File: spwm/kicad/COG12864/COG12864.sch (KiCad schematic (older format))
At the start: 12 parts, among them U1 N32G430C8L7, Y1 8MHZ

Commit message: adc_采样
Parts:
- added C? (x6): C, symbol Device:C
- added C?: CP, symbol Device:CP
- added D? (x2): 1N47xxA, Diode_THT:D_DO-41_SOD81_P10.16mm_Horizontal, symbol COG12864-cache:1N47xxA
- added D? (x10): 1N4148, Diode_THT:D_DO-35_SOD27_P7.62mm_Horizontal, symbol Diode:1N4148
- added D? (x4): 1N47xxA, Diode_THT:D_DO-41_SOD81_P10.16mm_Horizontal, symbol Diode:1N47xxA
- added Q? (x4): Q_NMOS_GDS, symbol Device:Q_NMOS_GDS
- added Q? (x4): SS8550, Package_TO_SOT_THT:TO-92_Inline, symbol Transistor_BJT:S8550
- added Q? (x2): SS8050, Package_TO_SOT_THT:TO-92_Inline, symbol Transistor_BJT:S8050
- added R? (x32): R, symbol Device:R
- added R?: 100, symbol Device:R
- added R? (x2): 10K, symbol Device:R
- added T? (x2): Transformer_1P_2S, symbol Device:Transformer_1P_2S
- added U? (x6): LM358, symbol Amplifier_Operational:LM358
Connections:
- net labels added: ADC1, PA9_TIM1_CH2, SIN
- wire segments 63 -> 279
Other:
- note added: "~"
- moved on the sheet: C1, C2, C3, C4, C5, C6, D1, DS1, J?, R1, U1, Y1

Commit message: 采样
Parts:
- removed C? (x6): C, symbol Device:C
- removed R? (x10): R, symbol Device:R
- removed R? (x2): 10K, symbol Device:R
- removed U? (x4): LM358, symbol Amplifier_Operational:LM358
- added C10, C7: 106, symbol Device:C
- added C9: C, symbol Device:C
- added D2, D3, D4, D5: 1N4148, Diode_THT:D_DO-35_SOD27_P7.62mm_Horizontal, symbol Diode:1N4148
- added R10, R28: 1K, symbol Device:R
- added R2, R3: 100K, symbol Device:R
- R4, R5: renamed from R?; value R -> 100
- R6, R7: renamed from R?; value R -> 1K
- R8, R9: renamed from R?; value R -> 100K
- U2: renamed from U?; value LM358 -> LMV722
- gave numbers to parts that had none: 47
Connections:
- wire segments 279 -> 269
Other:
- moved on the sheet: R4, R5, U2C

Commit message: 修改方案
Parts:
- removed D10, D11, D16, D17, D18, D19, D21, D7, D8, D9: 1N4148, Diode_THT:D_DO-35_SOD27_P7.62mm_Horizontal, symbol Diode:1N4148
- removed D12, D13, D14, D15: 1N47xxA, Diode_THT:D_DO-41_SOD81_P10.16mm_Horizontal, symbol Diode:1N47xxA
- removed D20, D6: 1N47xxA, Diode_THT:D_DO-41_SOD81_P10.16mm_Horizontal, symbol COG12864-cache:1N47xxA
- removed Q1, Q10: SS8050, Package_TO_SOT_THT:TO-92_Inline, symbol Transistor_BJT:S8050
- removed Q2, Q3, Q8, Q9: SS8550, Package_TO_SOT_THT:TO-92_Inline, symbol Transistor_BJT:S8550
- removed R15, R16, R17, R18, R19, R20, R21, R22, R23, R24, R25, R26, R27: R, symbol Device:R
- removed T1, T2: Transformer_1P_2S, symbol Device:Transformer_1P_2S
- added C11, C14: 104, symbol Device:C
- added C12, C13: 106, symbol Device:C
- added D10, D11: FR107, symbol Device:D
- added D6, D7, D8, D9: 1N4007, Diode_THT:D_DO-41_SOD81_P10.16mm_Horizontal, symbol Diode:1N4007
- added U3, U4: EG2131, symbol Driver_FET:IR2103
- R11, R13, R14: value R -> 33
- R12: value 100 -> 33
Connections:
- net labels added: PB13_TIM1_CH1N, PB14_TIM1_CH2N
- wire segments 269 -> 209
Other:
- moved on the sheet: C1, C2, C3, C4, C5, C6, D1, DS1, R1, U1, Y1

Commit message: 锁相成功
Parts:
- removed U2: LMV722, symbol Amplifier_Operational:LM358
- added C16, C?: 470UF, symbol Device:CP
- added R15: 900, symbol Device:R
- added R17: 100, symbol Device:R
- added R? (x2): R, symbol Device:R
- added U5: LMV722, symbol COG12864-cache:LMV358
- added U6: LMV722, symbol Regulator_Linear:LM317_TO-220
- C8: value CP -> 470UF
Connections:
- net labels added: PB6_TIM4_CH1_guoling
- wire segments 209 -> 231
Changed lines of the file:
@@
 Text Label 1500 2300 0    354  ~ 71
 SIN
-$Comp
-L Amplifier_Operational:LM358 U2
-U 1 1 632E71DB
-P 5450 3300
-F 0 "U2" H 5450 3667 50  0000 C CNN
-F 1 "LMV722" H 5450 3576 50  0000 C CNN
-F 2 "" H 5450 3300 50  0001 C CNN
-F 3 "http://www.ti.com/lit/ds/symlink/lm2904-n.pdf" H 5450 3300 50  0001 C CNN
-	1    5450 3300
-	1    0    0    1
-$EndComp
-$Comp
-L Amplifier_Operational:LM358 U2
-U 3 1 632EB879
-P 5700 5250
-F 0 "U2" V 5800 5200 50  0000 L CNN
-F 1 "LMV722" V 5700 5150 50  0000 L CNN
-F 2 "" H 5700 5250 50  0001 C CNN
-F 3 "http://www.ti.com/lit/ds/symlink/lm2904-n.pdf" H 5700 5250 50  0001 C CNN
-	3    5700 5250
-	0    -1   -1   0
-$EndComp
 Wire Wire Line
 	4650 2750 4300 2750
@@
 Wire Wire Line
 	6050 5150 6050 4750
-Connection ~ 5750 3300
 Text Label 5950 3300 0    50   ~ 0
 ADC0
@@
 	12750 5650 13150 5650
 Wire Wire Line
-	12450 6650 11750 6650
-Wire Wire Line
 	11750 6650 11750 6400
 Wire Wire Line
@@
 Wire Wire Line
 	11300 5600 11300 5450
-Wire Wire Line
-	11300 5450 11250 5450
 Wire Wire Line
 	11700 5500 11700 5600
@@
 P 10650 3950
 F 0 "C8" V 10395 3950 50  0000 C CNN
-F 1 "CP" V 10486 3950 50  0000 C CNN
+F 1 "470UF" V 10486 3950 50  0000 C CNN
 F 2 "" H 10688 3800 50  0001 C CNN
 F 3 "~" H 10650 3950 50  0001 C CNN
@@
 Wire Wire Line
 	10800 3950 11150 3950
-Wire Wire Line
-	11150 3950 11150 3800
 Wire Wire Line
 	11150 3200 11050 3200
@@
 	10000 3850 10000 3200
 Wire Wire Line
-	11250 5450 11250 3800
-Wire Wire Line
-	11250 3800 11150 3800
-Connection ~ 11250 5450
-Wire Wire Line
-	11250 5450 10900 5450
-Connection ~ 11150 3800
-Wire Wire Line
-	11150 3800 11150 3200
-Wire Wire Line
-	13450 5450 15250 5450
-Wire Wire Line
-	13450 7350 14550 7350
-Text Label 10700 6100 2    50   ~ 0
+	13450 5450 14350 5450
+Wire Wire Line
+	13450 7350 14350 7350
+Text Label 11050 6150 2    50   ~ 0
 PA8_TIM1_CH1
-Text Label 10700 6200 2    50   ~ 0
-PB13_TIM1_CH1N
-Wire Wire Line
-	11150 6100 10700 6100
-Wire Wire Line
-	11150 6200 10700 6200
 $Comp
 L Driver_FET:IR2103 U4
@@
 Wire Wire Line
 	15250 6300 15250 6450
-Wire Wire Line
-	17450 3800 11250 3800
-Connection ~ 11250 3800
 $Comp
 L power:GND #PWR020
@@
 Text Label 18000 6200 0    50   ~ 0
 PB14_TIM1_CH2N
+Wire Wire Line
+	11150 6100 11050 6100
+Wire Wire Line
+	11050 6100 11050 6200
+Wire Wire Line
+	11050 6200 11150 6200
+Wire Wire Line
+	10900 5450 11300 5450
+Wire Wire Line
+	11150 3200 11150 3950
+$Comp
+L Regulator_Linear:LM317_TO-220 U6
+U 1 1 62FA851E
+P 11450 3950
+F 0 "U6" H 11450 4192 50  0000 C CNN
+F 1 "LMV722" H 11450 4101 50  0000 C CNN
+F 2 "" H 11450 4200 50  0001 C CIN
+F 3 "" H 11450 3950 50  0001 C CNN
+	1    11450 3950
+	1    0    0    -1
+$EndComp
+Connection ~ 11150 3950
+$Comp
+L Device:R R17
+U 1 1 62FAA4DC
+P 11850 4100
+F 0 "R17" H 11920 4146 50  0000 L CNN
+F 1 "100" H 11920 4055 50  0000 L CNN
+F 2 "" V 11780 4100 50  0001 C CNN
+F 3 "~" H 11850 4100 50  0001 C CNN
+	1    11850 4100
+	1    0    0    -1
+$EndComp
+$Comp
+L Device:R R15
+U 1 1 62FAB838
+P 11450 4450
+F 0 "R15" H 11520 4496 50  0000 L CNN
+F 1 "900" H 11520 4405 50  0000 L CNN
+F 2 "" V 11380 4450 50  0001 C CNN
+F 3 "~" H 11450 4450 50  0001 C CNN
+	1    11450 4450
+	1    0    0    -1
+$EndComp
+$Comp
+L power:GND #PWR023
+U 1 1 62FACA5A
+P 11600 4600
+F 0 "#PWR023" H 11600 4350 50  0001 C CNN
+F 1 "GND" H 11605 4427 50  0000 C CNN
+F 2 "" H 11600 4600 50  0001 C CNN
+F 3 "" H 11600 4600 50  0001 C CNN
+	1    11600 4600
+	1    0    0    -1
+$EndComp
+$Comp
+L Device:CP C16
+U 1 1 62FAEE23
+P 12250 4100
+F 0 "C16" H 12368 4146 50  0000 L CNN
+F 1 "470UF" H 12368 4055 50  0000 L CNN
+F 2 "" H 12288 3950 50  0001 C CNN
+F 3 "~" H 12250 4100 50  0001 C CNN
+	1    12250 4100
+	1    0    0    -1
+$EndComp
+Wire Wire Line
+	11850 4250 11450 4250
+Wire Wire Line
+	11450 4300 11450 4250
+Connection ~ 11450 4250
+Wire Wire Line
+	12250 4250 12250 4600
+Wire Wire Line
+	12250 4600 11600 4600
+Connection ~ 11600 4600
+Wire Wire Line
+	11600 4600 11450 4600
+Wire Wire Line
+	11750 3950 11850 3950
+Wire Wire Line
+	12750 3950 12750 5100
+Wire Wire Line
+	12750 5100 10900 5100
+Wire Wire Line
+	10900 5100 10900 5450
+Connection ~ 11850 3950
+Wire Wire Line
+	11850 3950 12250 3950
+Connection ~ 12250 3950
+Wire Wire Line
+	12250 3950 12750 3950
+Connection ~ 10900 5450
+Wire Wire Line
+	17450 3800 12750 3800
+Wire Wire Line
+	12750 3800 12750 3950
+Connection ~ 12750 3950
+$Comp
+L COG12864-cache:LMV358 U5
+U 1 1 63029AA7
+P 5450 3300
+F 0 "U5" H 5450 2933 50  0000 C CNN
+F 1 "LMV722" H 5450 3024 50  0000 C CNN
+F 2 "" H 5450 3300 50  0001 C CNN
+F 3 "" H 5450 3300 50  0001 C CNN
+	1    5450 3300
+	1    0    0    1
+$EndComp
+Connection ~ 5750 3300
+$Comp
+L COG12864-cache:LMV358 U5
+U 2 1 63040D47
+P 2500 3350
+F 0 "U5" H 2500 3717 50  0000 C CNN
+F 1 "LMV722" H 2500 3626 50  0000 C CNN
+F 2 "" H 2500 3350 50  0001 C CNN
+F 3 "" H 2500 3350 50  0001 C CNN
+	2    2500 3350
+	-1   0    0    -1
+$EndComp
+$Comp
+L COG12864-cache:LMV358 U5
+U 3 1 6306A874
+P 5700 5450
+F 0 "U5" V 5375 5450 50  0000 C CNN
+F 1 "LMV722" V 5466 5450 50  0000 C CNN
+F 2 "" H 5700 5450 50  0001 C CNN
+F 3 "" H 5700 5450 50  0001 C CNN
+	3    5700 5450
+	0    1    1    0
+$EndComp
+$Comp
+L Device:R R?
+U 1 1 630829B4
+P 3050 2650
+F 0 "R?" V 3257 2650 50  0000 C CNN
+F 1 "R" V 3166 2650 50  0000 C CNN
+F 2 "" V 2980 2650 50  0001 C CNN
+F 3 "~" H 3050 2650 50  0001 C CNN
+	1    3050 2650
+	0    -1   -1   0
+$EndComp
+$Comp
+L Device:R R?
+U 1 1 630A335E
+P 3100 3800
+F 0 "R?" V 2893 3800 50  0000 C CNN
+F 1 "R" V 2984 3800 50  0000 C CNN
+F 2 "" V 3030 3800 50  0001 C CNN
+F 3 "~" H 3100 3800 50  0001 C CNN
+	1    3100 3800
+	0    1    1    0
+$EndComp
+Wire Wire Line
+	3250 3800 3350 3800
+Connection ~ 3350 3800
+Wire Wire Line
+	2950 3800 2800 3800
+Wire Wire Line
+	2800 3800 2800 3450
+Wire Wire Line
+	2800 3250 2800 2650
+Wire Wire Line
+	2800 2650 2900 2650
+Wire Wire Line
+	3200 2650 3750 2650
+Text Label 2100 3350 2    50   ~ 0
+PB6_TIM4_CH1_guoling
+Wire Wire Line
+	2200 3350 2100 3350
+Text Label 8900 10150 0    50   ~ 0
+PB6_TIM4_CH1_guoling
+Wire Wire Line
+	7050 11200 6950 11200
+Wire Wire Line
+	11750 6650 12450 6650
+$Comp
+L Device:CP C?
+U 1 1 63178030
+P 14350 6300
+F 0 "C?" H 14468 6346 50  0000 L CNN
+F 1 "470UF" H 14468 6255 50  0000 L CNN
+F 2 "" H 14388 6150 50  0001 C CNN
+F 3 "~" H 14350 6300 50  0001 C CNN
+	1    14350 6300
+	1    0    0    -1
+$EndComp
+Wire Wire Line
+	14350 6150 14350 5450
+Connection ~ 14350 5450
+Wire Wire Line
+	14350 5450 15250 5450
+Wire Wire Line
+	14350 6450 14350 7350
+Connection ~ 14350 7350
+Wire Wire Line
+	14350 7350 14550 7350
+Wire Wire Line
+	8850 10150 9000 10150
 $EndSCHEMATC

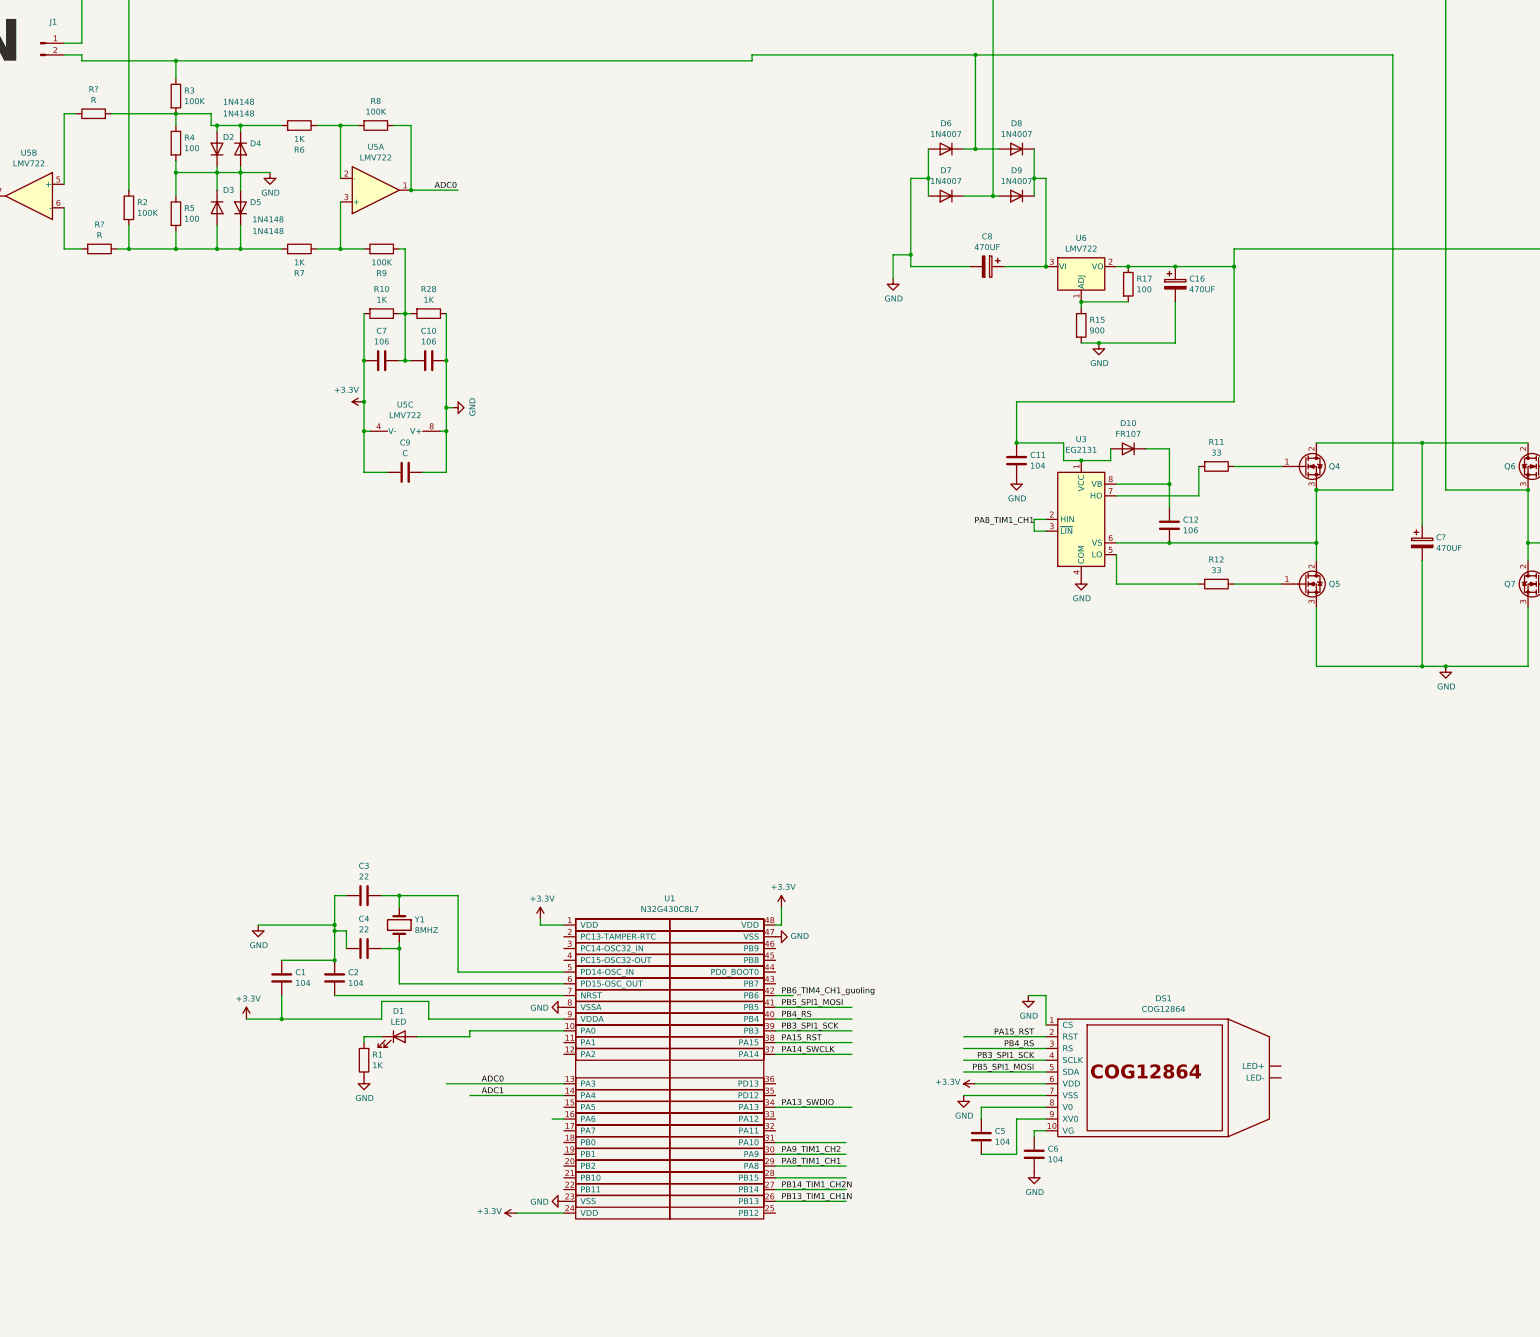
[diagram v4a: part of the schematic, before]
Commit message: 可调相位振幅
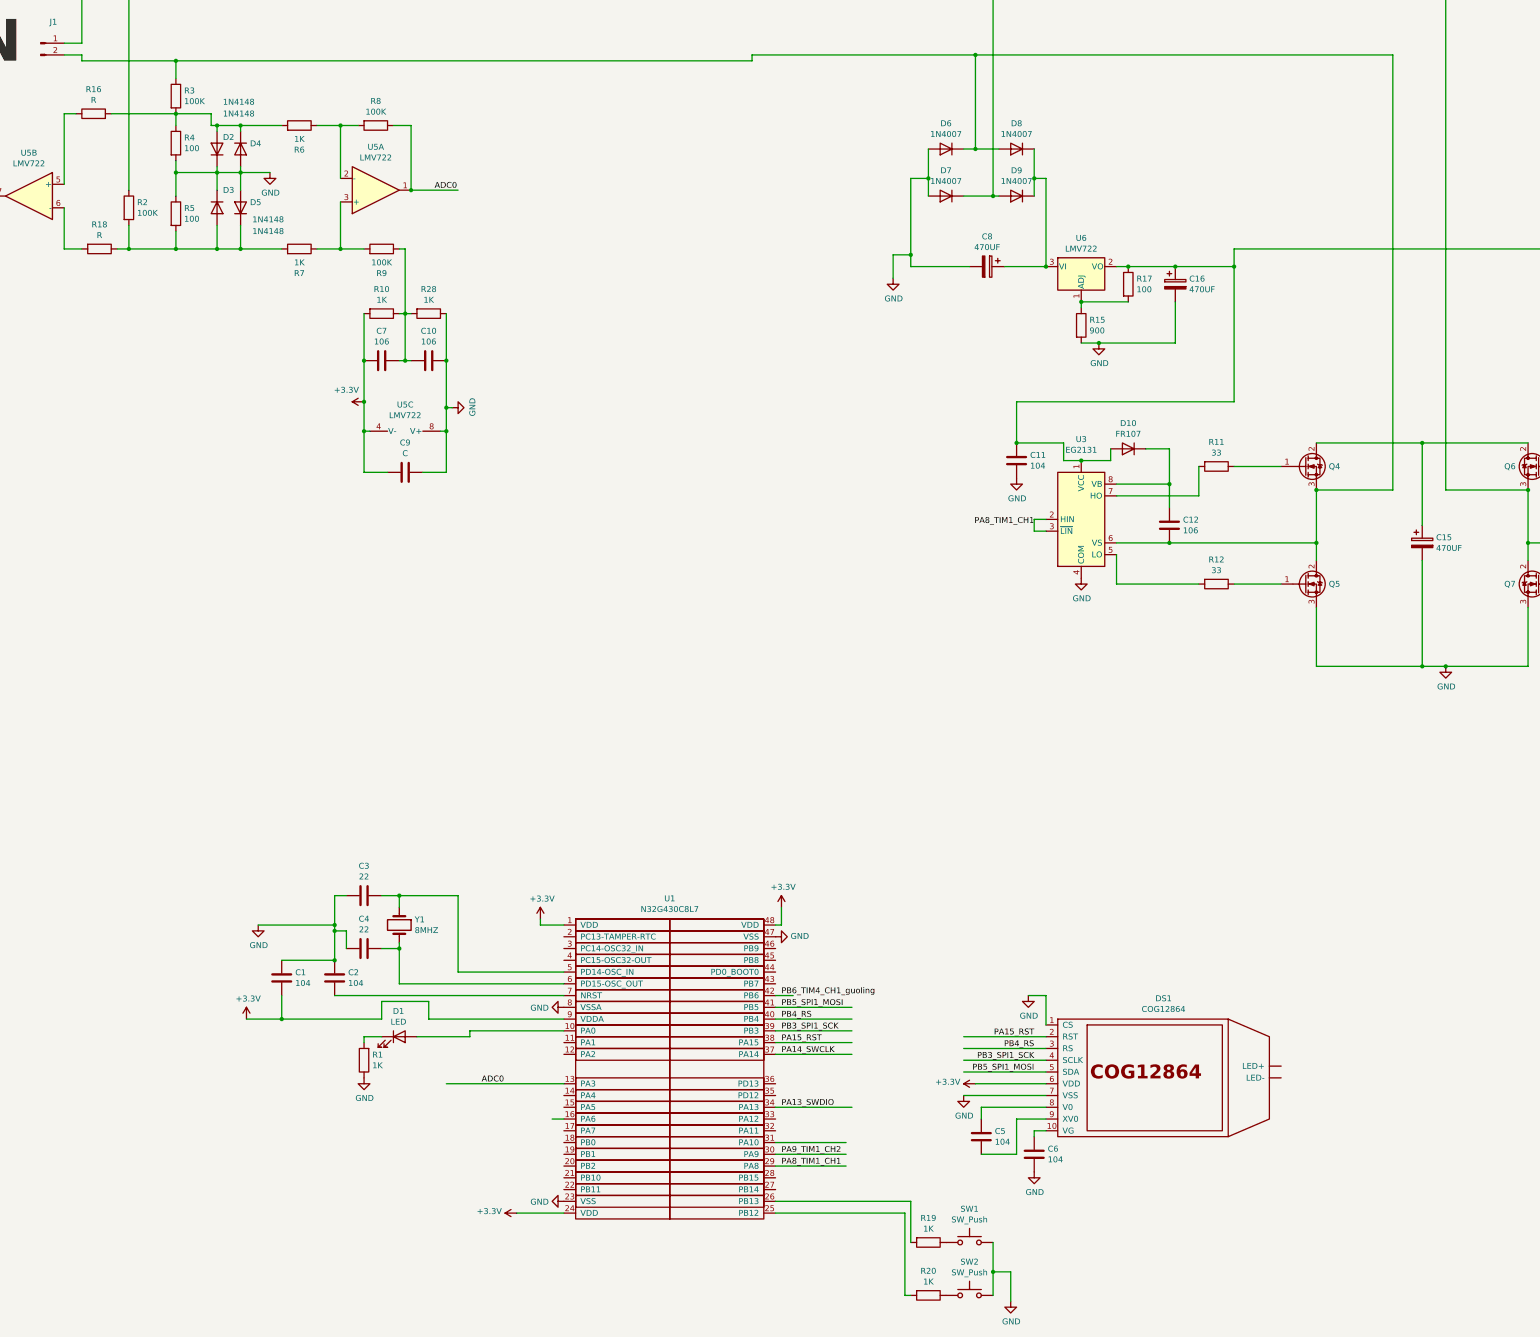
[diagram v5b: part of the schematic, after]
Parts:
- added R19, R20: 1K, symbol Device:R
- added SW1, SW2: SW_Push, symbol Switch:SW_Push
- gave numbers to parts that had none: 3
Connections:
- net labels removed: ADC1, PB13_TIM1_CH1N
- wire segments 231 -> 236
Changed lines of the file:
@@
 ADC0
-Wire Wire Line
-	8850 11700 9450 11700
-Wire Wire Line
-	8850 11900 9450 11900
-Wire Wire Line
-	8850 11800 9450 11800
 Wire Wire Line
 	8850 11500 9450 11500
@@
 	1    0    0    -1
 $EndComp
-Text Label 6350 11000 0    50   ~ 0
-ADC1
-Wire Wire Line
-	6250 11000 7050 11000
 Wire Wire Line
 	6050 10900 7050 10900
@@
 Wire Wire Line
 	8850 11600 9450 11600
-Text Label 8900 11900 0    50   ~ 0
-PB13_TIM1_CH1N
-Text Label 8900 11800 0    50   ~ 0
-PB14_TIM1_CH2N
 $Comp
 L Driver_FET:IR2103 U3
@@
 $EndComp
 $Comp
-L Device:R R?
+L Device:R R16
 U 1 1 630829B4
 P 3050 2650
-F 0 "R?" V 3257 2650 50  0000 C CNN
+F 0 "R16" V 3257 2650 50  0000 C CNN
 F 1 "R" V 3166 2650 50  0000 C CNN
 F 2 "" V 2980 2650 50  0001 C CNN
@@
 $EndComp
 $Comp
-L Device:R R?
+L Device:R R18
 U 1 1 630A335E
 P 3100 3800
-F 0 "R?" V 2893 3800 50  0000 C CNN
+F 0 "R18" V 2893 3800 50  0000 C CNN
 F 1 "R" V 2984 3800 50  0000 C CNN
 F 2 "" V 3030 3800 50  0001 C CNN
@@
 	11750 6650 12450 6650
 $Comp
-L Device:CP C?
+L Device:CP C15
 U 1 1 63178030
 P 14350 6300
-F 0 "C?" H 14468 6346 50  0000 L CNN
+F 0 "C15" H 14468 6346 50  0000 L CNN
 F 1 "470UF" H 14468 6255 50  0000 L CNN
 F 2 "" H 14388 6150 50  0001 C CNN
@@
 Wire Wire Line
 	8850 10150 9000 10150
+$Comp
+L Switch:SW_Push SW1
+U 1 1 62FC7418
+P 10500 12250
+F 0 "SW1" H 10500 12535 50  0000 C CNN
+F 1 "SW_Push" H 10500 12444 50  0000 C CNN
+F 2 "" H 10500 12450 50  0001 C CNN
+F 3 "~" H 10500 12450 50  0001 C CNN
+	1    10500 12250
+	1    0    0    -1
+$EndComp
+$Comp
+L Switch:SW_Push SW2
+U 1 1 62FC8C6B
+P 10500 12700
+F 0 "SW2" H 10500 12985 50  0000 C CNN
+F 1 "SW_Push" H 10500 12894 50  0000 C CNN
+F 2 "" H 10500 12900 50  0001 C CNN
+F 3 "~" H 10500 12900 50  0001 C CNN
+	1    10500 12700
+	1    0    0    -1
+$EndComp
+$Comp
+L Device:R R19
+U 1 1 63014C5F
+P 10150 12250
+F 0 "R19" V 9943 12250 50  0000 C CNN
+F 1 "1K" V 10034 12250 50  0000 C CNN
+F 2 "" V 10080 12250 50  0001 C CNN
+F 3 "~" H 10150 12250 50  0001 C CNN
+	1    10150 12250
+	0    1    1    0
+$EndComp
+$Comp
+L Device:R R20
+U 1 1 630169B6
+P 10150 12700
+F 0 "R20" V 9943 12700 50  0000 C CNN
+F 1 "1K" V 10034 12700 50  0000 C CNN
+F 2 "" V 10080 12700 50  0001 C CNN
+F 3 "~" H 10150 12700 50  0001 C CNN
+	1    10150 12700
+	0    1    1    0
+$EndComp
+Wire Wire Line
+	10700 12250 10700 12500
+$Comp
+L power:GND #PWR024
+U 1 1 6304417B
+P 10850 12750
+F 0 "#PWR024" H 10850 12500 50  0001 C CNN
+F 1 "GND" H 10855 12577 50  0000 C CNN
+F 2 "" H 10850 12750 50  0001 C CNN
+F 3 "" H 10850 12750 50  0001 C CNN
+	1    10850 12750
+	1    0    0    -1
+$EndComp
+Wire Wire Line
+	10850 12750 10850 12500
+Wire Wire Line
+	10850 12500 10700 12500
+Connection ~ 10700 12500
+Wire Wire Line
+	10700 12500 10700 12700
+Wire Wire Line
+	9950 12700 10000 12700
+Wire Wire Line
+	8850 11900 10000 11900
+Wire Wire Line
+	10000 11900 10000 12250
+Wire Wire Line
+	8850 12000 9950 12000
+Wire Wire Line
+	9950 12000 9950 12700
 $EndSCHEMATC
